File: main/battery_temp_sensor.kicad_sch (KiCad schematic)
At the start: 5 parts

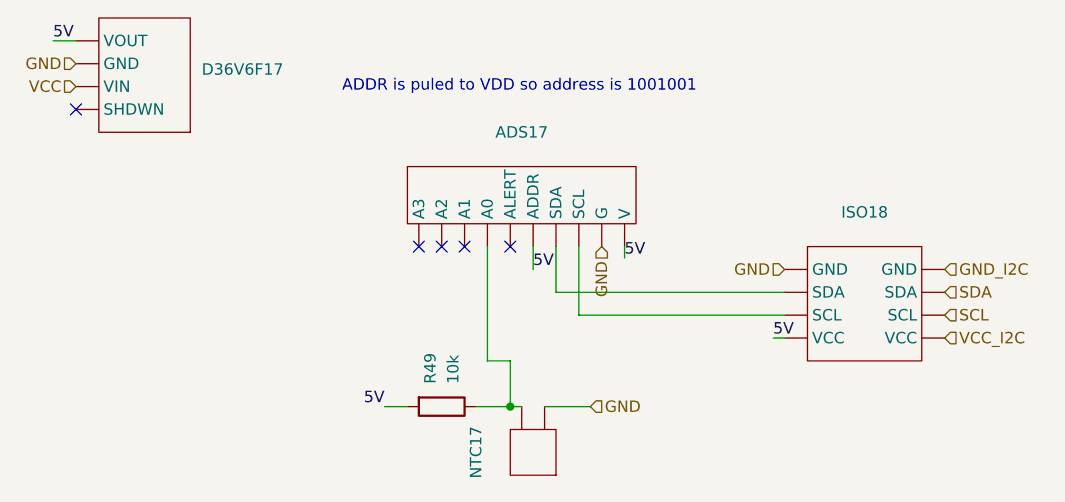
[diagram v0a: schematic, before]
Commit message: Added MPU6050 and GPS Module to CCU
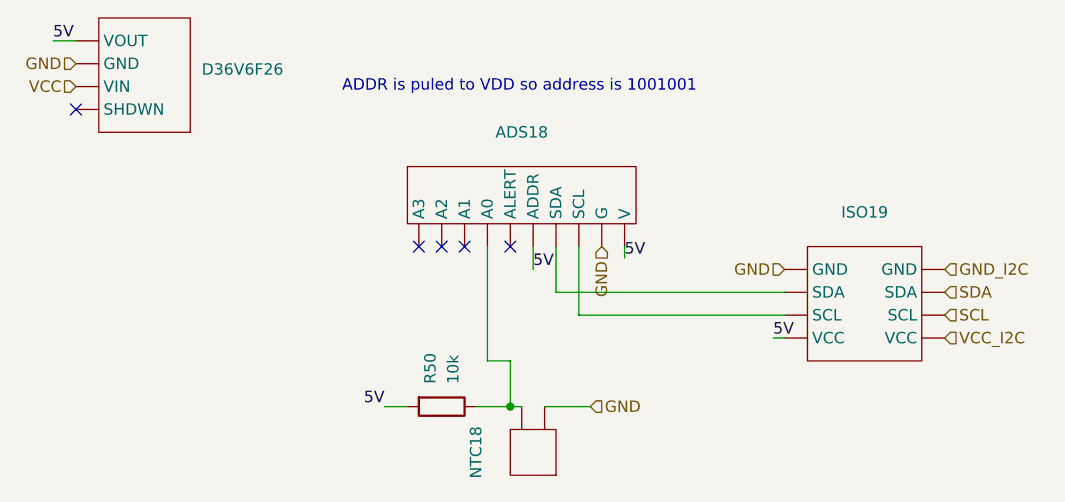
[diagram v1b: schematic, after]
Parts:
- renumbered ADS17 to ADS18, D36V6F17 to D36V6F26, ISO18 to ISO19, NTC17 to NTC18, R49 to R50
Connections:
- new net: ADS18. (V), NTC18., R50.1
- new net: ADS18. (V), ISO19. (VCC) (x2)
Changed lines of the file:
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@@
 		(dnp no)
 		(fields_autoplaced yes)
-		(property "Reference" "ADS17"
+		(property "Reference" "ADS18"
 			(at 97.79 54.61 0)
 			(effects
@@
 		(dnp no)
 		(fields_autoplaced yes)
-		(property "Reference" "NTC17"
+		(property "Reference" "NTC18"
 			(at 92.71 90.17 90)
 			(effects
@@
 		(dnp no)
 		(fields_autoplaced yes)
-		(property "Reference" "ISO18"
+		(property "Reference" "ISO19"
 			(at 135.89 63.5 0)
 			(effects
@@
 		(dnp no)
 		(fields_autoplaced yes)
-		(property "Reference" "R49"
+		(property "Reference" "R50"
 			(at 87.6299 82.55 0)
 			(effects
@@
 		(dnp no)
 		(fields_autoplaced yes)
-		(property "Reference" "D36V6F17"
+		(property "Reference" "D36V6F26"
 			(at 62.23 47.6249 0)
 			(effects

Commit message: added logos, oranised sheets, final version
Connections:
- new net: ADS18. (V), NTC18., R50.1
- new net: ADS18. (V), ISO19. (VCC) (x2)
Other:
- company: (none) -> Designers: Krzysztof Grajek, Wojtek Kołodziej

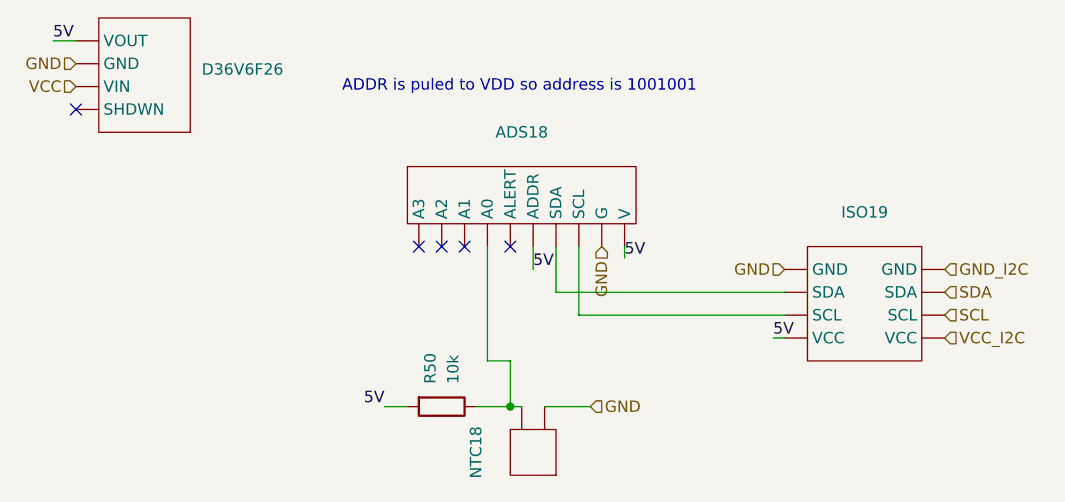
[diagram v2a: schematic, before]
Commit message: Changed name of Adafruit 4903(i2c spearator). Changed values of resistors used in panels
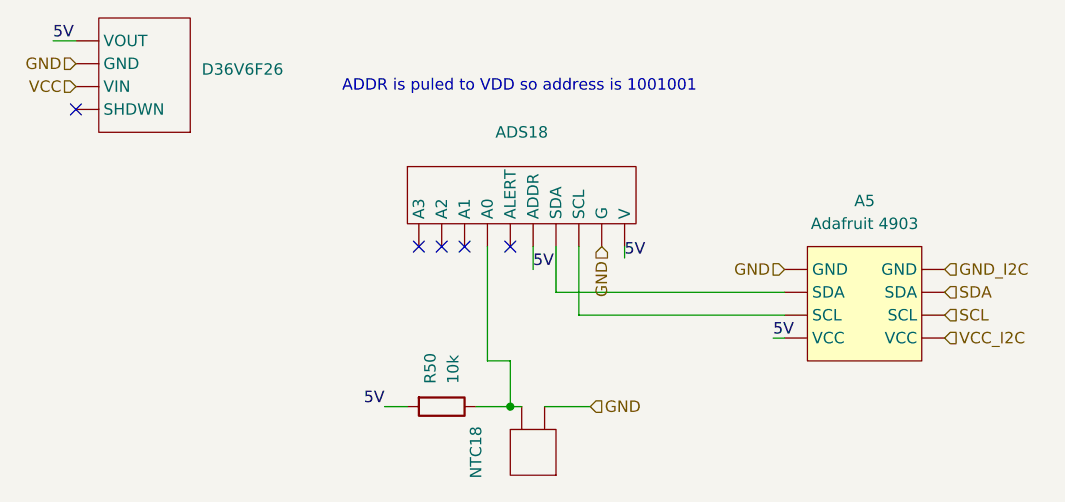
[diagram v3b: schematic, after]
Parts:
- removed ISO19: ~, symbol New_Library_0:Bidirectional I2C Isolator
- added A5: Adafruit 4903, symbol New_Library_0:Adafruit_4903
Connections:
- net 5V: now also A5. (VCC)
- net GND: now also A5. (VCC)
- net GND_I2C: now also A5. (VCC)
- net SCL: now also A5. (VCC)
- net SDA: now also A5. (VCC)
- net VCC_I2C: now also A5. (VCC)
- new net: ADS18. (V), NTC18., R50.1
- new net: A5. (VCC), ADS18. (V) (x2)
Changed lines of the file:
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@@
-	)
-	(symbol
-		(lib_id "New_Library_0:Bidirectional I2C Isolator")
-		(at 135.89 73.66 0)
-		(unit 1)
-		(exclude_from_sim no)
-		(in_bom yes)
-		(on_board yes)
-		(dnp no)
-		(fields_autoplaced yes)
-		(property "Reference" "ISO19"
-			(at 135.89 63.5 0)
-			(effects
-				(font
-					(size 1.27 1.27)
-				)
-			)
-		)
-		(property "Value" "~"
-			(at 135.89 66.04 0)
-			(effects
-				(font
-					(size 1.27 1.27)
-				)
-			)
-		)
-		(property "Footprint" ""
-			(at 135.89 80.01 0)
-			(effects
-				(font
-					(size 1.27 1.27)
-				)
-				(hide yes)
-			)
-		)
-		(property "Datasheet" ""
-			(at 135.89 80.01 0)
-			(effects
-				(font
-					(size 1.27 1.27)
-				)
-				(hide yes)
-			)
-		)
-		(property "Description" ""
-			(at 135.89 80.01 0)
-			(effects
-				(font
-					(size 1.27 1.27)
-				)
-				(hide yes)
-			)
-		)
-		(pin ""
-		)
-		(pin ""
-		)
-		(pin ""
-		)
-		(pin ""
-		)
-		(pin ""
-		)
-		(pin ""
-		)
-		(pin ""
-		)
-		(pin ""
-		)
-		(instances
-			(project "main"
-				(path "/54fbbba9-a737-4199-9a4b-f9fa49b3de5e/956e0365-6d74-4799-9d68-b1a004ee179e/eeb18b0a-49a7-4ad2-b2b8-4d198a13df29/0bcc56e3-8735-4d1a-a350-1ae9e845a70b"
-					(reference "ISO19")
-					(unit 1)
-				)
-				(path "/54fbbba9-a737-4199-9a4b-f9fa49b3de5e/956e0365-6d74-4799-9d68-b1a004ee179e/eeb18b0a-49a7-4ad2-b2b8-4d198a13df29/5a388ad5-d7e4-450e-90e4-439ec71463dc"
-					(reference "ISO18")
-					(unit 1)
-				)
-			)
-		)
 	)
 	(symbol
@@
 					(unit 1)
 				)
+			)
+		)
+	)
+	(symbol
+		(lib_id "New_Library_0:Adafruit_4903")
+		(at 135.89 73.66 0)
+		(unit 1)
+		(exclude_from_sim no)
+		(in_bom yes)
+		(on_board yes)
+		(dnp no)
+		(fields_autoplaced yes)
+		(property "Reference" "A5"
+			(at 135.89 62.23 0)
+			(effects
+				(font
+					(size 1.27 1.27)
+				)
+			)
+		)
+		(property "Value" "Adafruit 4903"
+			(at 135.89 64.77 0)
+			(effects
+				(font
+					(size 1.27 1.27)
+				)
+			)
+		)
+		(property "Footprint" ""
+			(at 135.89 80.01 0)
+			(effects
+				(font
+					(size 1.27 1.27)
+				)
+				(hide yes)
+			)
+		)
+		(property "Datasheet" ""
+			(at 135.89 80.01 0)
+			(effects
+				(font
+					(size 1.27 1.27)
+				)
+				(hide yes)
+			)
+		)
+		(property "Description" ""
+			(at 135.89 80.01 0)
+			(effects
+				(font
+					(size 1.27 1.27)
+				)
+				(hide yes)
+			)
+		)
+		(pin ""
+		)
+		(pin ""
+		)
+		(pin ""
+		)
+		(pin ""
+		)
+		(pin ""
+		)
+		(pin ""
+		)
+		(pin ""
+		)
+		(pin ""
+		)
+		(instances
+			(project ""
+				(path "/54fbbba9-a737-4199-9a4b-f9fa49b3de5e/956e0365-6d74-4799-9d68-b1a004ee179e/eeb18b0a-49a7-4ad2-b2b8-4d198a13df29/0bcc56e3-8735-4d1a-a350-1ae9e845a70b"
+					(reference "A5")
+					(unit 1)
+				)
+				(path "/54fbbba9-a737-4199-9a4b-f9fa49b3de5e/956e0365-6d74-4799-9d68-b1a004ee179e/eeb18b0a-49a7-4ad2-b2b8-4d198a13df29/5a388ad5-d7e4-450e-90e4-439ec71463dc"
+					(reference "A1")
+					(unit 1)
+				)
